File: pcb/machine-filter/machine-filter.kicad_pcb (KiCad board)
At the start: 2 copper layers, 150 x 107 mm, 156 parts, among them J1 PJ398SM, J10 PJ398SM, J11 PJ398SM, J12 PJ398SM, J13 EURO PWR 2x5, J14 EXPANSION 2x4, J15 TF-01A, J2 PJ398SM, J3 PJ398SM, J4 PJ398SM, J5 PJ398SM, J6 PJ398SM, J7 PJ398SM, J8 PJ398SM, J9 PJ398SM, U1 LMV324, U2 LMV324, U3 TL072, U4 TL072, U5 LM4040-10, U6 74HC4051, U7 LM324, U8 LM324

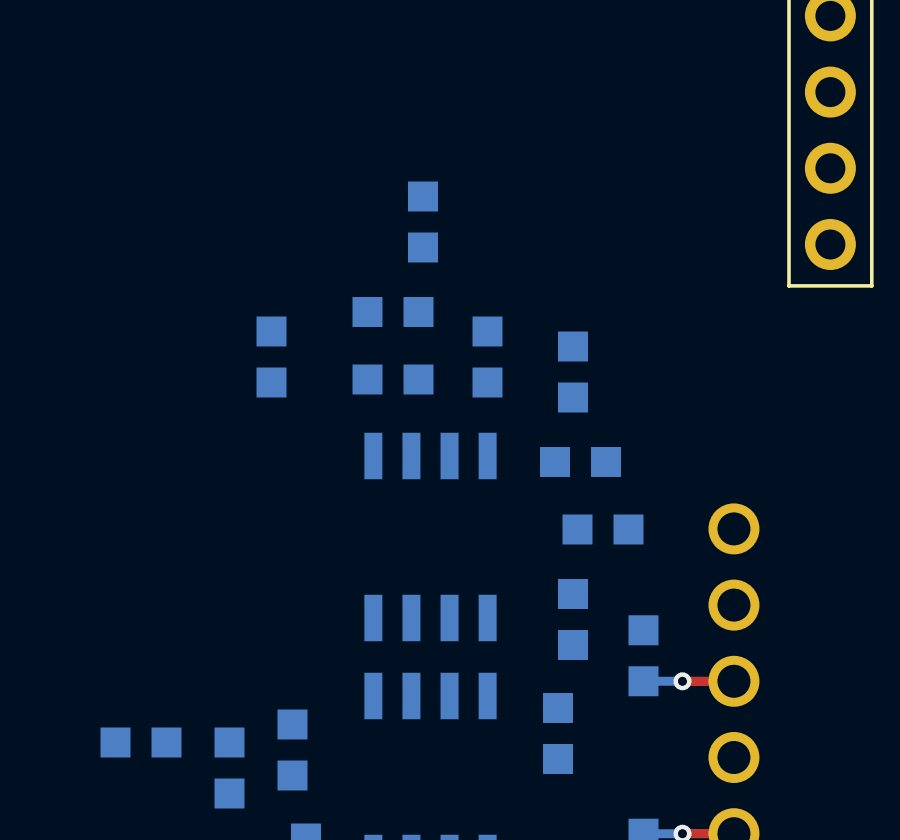
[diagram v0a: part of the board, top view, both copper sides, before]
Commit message: Section audio out (U4) by pattern; render_board.py for whole-board pictures
Co-Authored-By: Claude Opus 5.5 <noreply@anthropic.com>
Claude-Session: https://claude.ai/code/session_01Cf5qNBi3oNHhbCjPHvswth
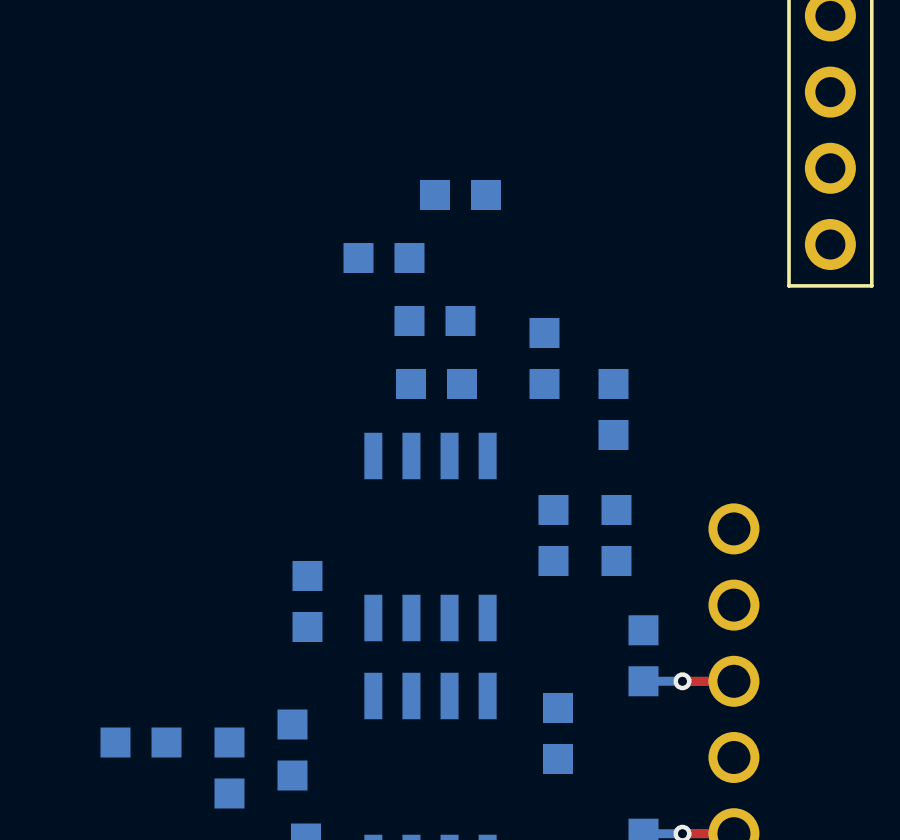
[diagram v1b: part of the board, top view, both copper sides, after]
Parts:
- moved R64 9.44 mm to (201.9, 82.2), turned to 0 degrees
- moved C73 8.24 mm to (199.4, 93.7)
- moved R61 2.87 mm to (207.6, 91.5), turned to -90 degrees
- moved C72 1.90 mm to (207.3, 85.5), turned to -90 degrees
- moved R62 1.84 mm to (209.6, 87.2)
- moved R66 1.54 mm to (204.5, 80.1), turned to 0 degrees
- moved R65 1.46 mm to (203.7, 86.4)
- moved C62 1.43 mm to (203.7, 84.3)
- moved C60 0.49 mm to (209.7, 91.5), turned to -90 degrees

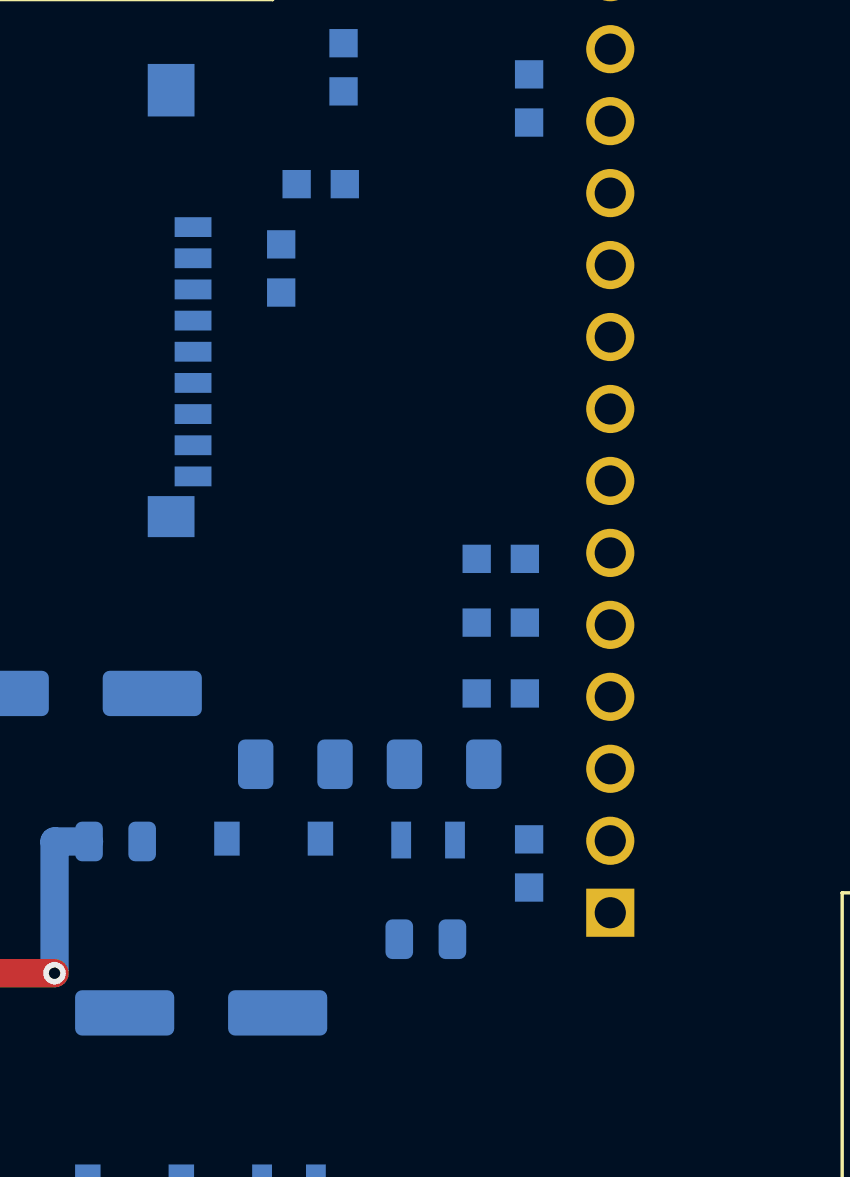
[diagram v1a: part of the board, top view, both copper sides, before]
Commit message: Section microSD: pull-ups as a column beside the Seed3 SD pins, C100 at J15's supply pin
Co-Authored-By: Claude Opus 5.5 <noreply@anthropic.com>
Claude-Session: https://claude.ai/code/session_01Cf5qNBi3oNHhbCjPHvswth
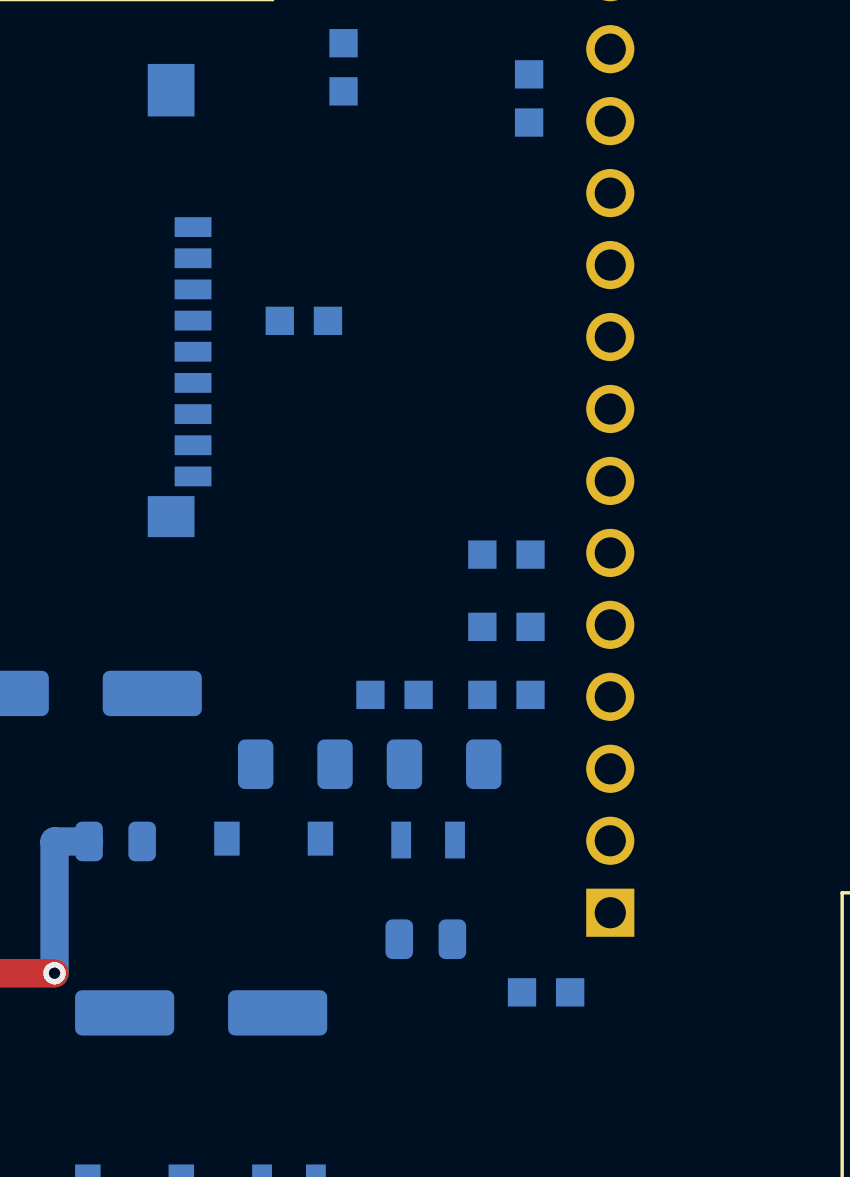
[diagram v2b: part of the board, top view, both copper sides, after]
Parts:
- moved R100 15.6 mm to (206.0, 131.8), turned to 180 degrees
- moved C100 4.86 mm to (202.8, 118.6)
- moved R101 4.59 mm to (211.3, 142.3), turned to 180 degrees
- moved R102 0.25 mm to (209.9, 126.8)
- moved R103 0.25 mm to (209.9, 129.4)
- moved R104 0.21 mm to (209.9, 131.8)
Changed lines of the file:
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@@
 	(footprint "filter-module:R_0603"
 		(layer "B.Cu")
-		(at 209.75 131.75 180)
+		(at 209.95 131.8 180)
 		(descr "Resistor SMD 0603, reflow soldering, Vishay (see dcrcw.pdf)")
 		(tags "resistor 0603")
@@
 	(footprint "filter-module:C_0603"
 		(layer "B.Cu")
-		(at 203.395 113.775)
+		(at 202.8 118.6)
 		(descr "Capacitor SMD 0603, reflow soldering, AVX (see smccp.pdf)")
 		(tags "capacitor 0603 C0603")
@@
 	(footprint "filter-module:R_0603"
 		(layer "B.Cu")
-		(at 209.75 127 180)
+		(at 209.95 126.85 180)
 		(descr "Resistor SMD 0603, reflow soldering, Vishay (see dcrcw.pdf)")
 		(tags "resistor 0603")
@@
 	(footprint "filter-module:R_0603"
 		(layer "B.Cu")
-		(at 209.75 129.25 180)
+		(at 209.95 129.4 180)
 		(descr "Resistor SMD 0603, reflow soldering, Vishay (see dcrcw.pdf)")
 		(tags "resistor 0603")
@@
 	(footprint "filter-module:R_0603"
 		(layer "B.Cu")
-		(at 202 116.75 -90)
+		(at 206 131.8 180)
 		(descr "Resistor SMD 0603, reflow soldering, Vishay (see dcrcw.pdf)")
 		(tags "resistor 0603")
 		(property "Reference" "R100"
-			(at 0 1.449999 90)
+			(at 0 1.449999 0)
 			(unlocked yes)
 			(layer "B.SilkS")
@@
 		)
 		(property "Value" "47k"
-			(at 0 -1.45 90)
+			(at 0 -1.45 0)
 			(unlocked yes)
 			(layer "B.SilkS")
@@
 		)
 		(property "Datasheet" ""
-			(at 0 0 90)
+			(at 0 0 0)
 			(layer "B.Fab")
 			(hide yes)
@@
 		)
 		(property "Description" ""
-			(at 0 0 90)
+			(at 0 0 0)
 			(layer "B.Fab")
 			(hide yes)
@@
 		(duplicate_pad_numbers_are_jumpers no)
 		(fp_line
-			(start -0.85 0.699999)
-			(end 0.85 0.699999)
+			(start 0.85 -0.7)
+			(end -0.85 -0.7)
 			(stroke
 				(width 0.12)
@@
 		)
 		(fp_line
-			(start 0.85 -0.7)
-			(end -0.85 -0.7)
+			(start -0.85 0.699999)
+			(end 0.85 0.699999)
 			(stroke
 				(width 0.12)
@@
 		)
 		(fp_line
-			(start -1.6 0.75)
-			(end 1.6 0.75)
+			(start 1.6 0.75)
+			(end 1.6 -0.75)
 			(stroke
 				(width 0.05)
@@
 		(fp_line
 			(start -1.6 0.75)
-			(end -1.6 -0.75)
+			(end 1.6 0.75)
 			(stroke
 				(width 0.05)
@@
 		)
 		(fp_line
-			(start 1.6 0.75)
-			(end 1.6 -0.75)
+			(start -1.6 0.75)
+			(end -1.6 -0.75)
 			(stroke
 				(width 0.05)
@@
 		)
 		(pad "1" smd rect
-			(at -0.85 0 270)
+			(at -0.85 0 180)
 			(size 1 1)
 			(layers "B.Cu" "B.Mask" "B.Paste")
@@
 		)
 		(pad "2" smd rect
-			(at 0.85 0 270)
+			(at 0.85 0 180)
 			(size 1 1)
 			(layers "B.Cu" "B.Mask" "B.Paste")
@@
 	(footprint "filter-module:R_0603"
 		(layer "B.Cu")
-		(at 210.75 137.75 -90)
+		(at 211.35 142.3 180)
 		(descr "Resistor SMD 0603, reflow soldering, Vishay (see dcrcw.pdf)")
 		(tags "resistor 0603")
 		(property "Reference" "R101"
-			(at 0 1.449999 90)
+			(at 0 1.449999 0)
 			(unlocked yes)
 			(layer "B.SilkS")
@@
 		)
 		(property "Value" "47k"
-			(at 0 -1.45 90)
+			(at 0 -1.45 0)
 			(unlocked yes)
 			(layer "B.SilkS")
@@
 		)
 		(property "Datasheet" ""
-			(at 0 0 90)
+			(at 0 0 0)
 			(layer "B.Fab")
 			(hide yes)
@@
 		)
 		(property "Description" ""
-			(at 0 0 90)
+			(at 0 0 0)
 			(layer "B.Fab")
 			(hide yes)
@@
 		(duplicate_pad_numbers_are_jumpers no)
 		(fp_line
-			(start -0.85 0.699999)
-			(end 0.85 0.699999)
+			(start 0.85 -0.7)
+			(end -0.85 -0.7)
 			(stroke
 				(width 0.12)
@@
 		)
 		(fp_line
-			(start 0.85 -0.7)
-			(end -0.85 -0.7)
+			(start -0.85 0.699999)
+			(end 0.85 0.699999)
 			(stroke
 				(width 0.12)
@@
 		)
 		(fp_line
-			(start -1.6 0.75)
-			(end 1.6 0.75)
+			(start 1.6 0.75)
+			(end 1.6 -0.75)
 			(stroke
 				(width 0.05)
@@
 		(fp_line
 			(start -1.6 0.75)
-			(end -1.6 -0.75)
+			(end 1.6 0.75)
 			(stroke
 				(width 0.05)
@@
 		)
 		(fp_line
-			(start 1.6 0.75)
-			(end 1.6 -0.75)
+			(start -1.6 0.75)
+			(end -1.6 -0.75)
 			(stroke
 				(width 0.05)
@@
 		)
 		(pad "1" smd rect
-			(at -0.85 0 270)
+			(at -0.85 0 180)
 			(size 1 1)
 			(layers "B.Cu" "B.Mask" "B.Paste")
@@
 		)
 		(pad "2" smd rect
-			(at 0.85 0 270)
+			(at 0.85 0 180)
 			(size 1 1)
 			(layers "B.Cu" "B.Mask" "B.Paste")

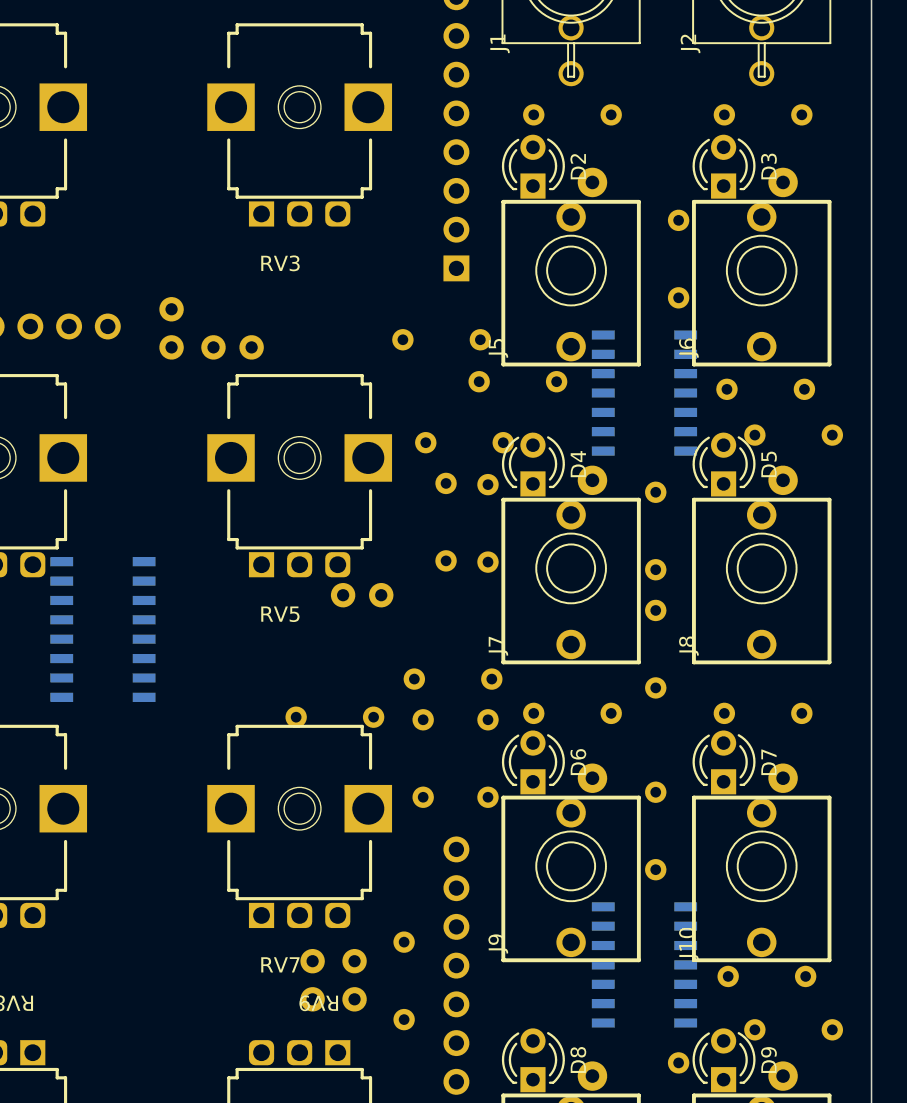
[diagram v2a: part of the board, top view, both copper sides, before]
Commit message: Control sections U6 and U7: decouplers at their supply pins; U7's resistors re-placed around them
The bank pattern doesn't fit between the jacks (parts landed 6-14 mm off), so U7's resistors keep the
shortest-connection placement (auto_place), re-run after the decouplers moved.

Co-Authored-By: Claude Opus 5.5 <noreply@anthropic.com>
Claude-Session: https://claude.ai/code/session_01Cf5qNBi3oNHhbCjPHvswth
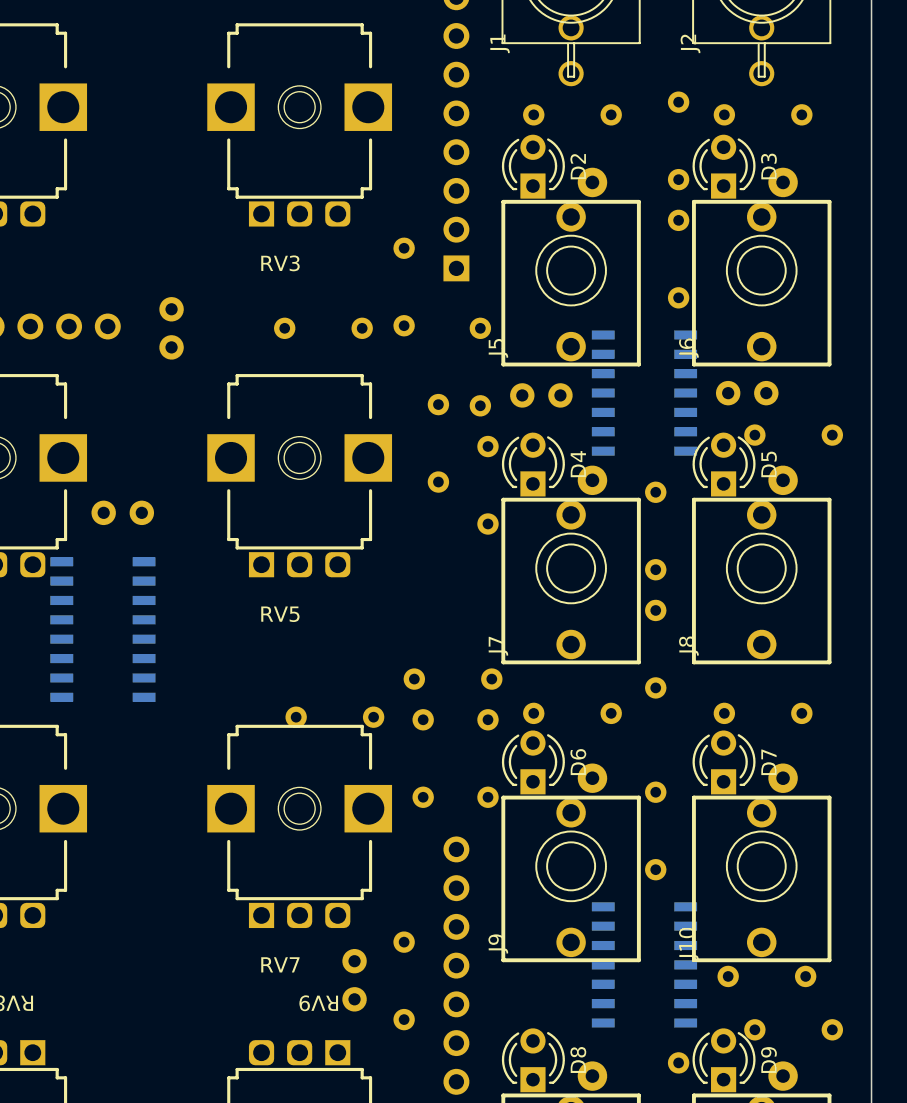
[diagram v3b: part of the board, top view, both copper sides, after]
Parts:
- moved C82 39.6 mm to (147.5, 110.4), turned to 0 degrees
- moved C81 33.9 mm to (161.0, 110.2)
- moved R83 20.7 mm to (139.8, 100.8), turned to -90 degrees
- moved C80 16.6 mm to (120.0, 118.1)
- moved R93 13.2 mm to (137.0, 106.0), turned to 180 degrees
- moved R81 10.2 mm to (157.8, 104.0), turned to 90 degrees
- moved R91 7.75 mm to (157.8, 96.2)
- moved R80 6.10 mm to (144.8, 106.0), turned to -90 degrees
- moved R90 5.06 mm to (142.0, 111.0), turned to -90 degrees
- moved R73 1.03 mm to (145.2, 113.8), turned to -90 degrees

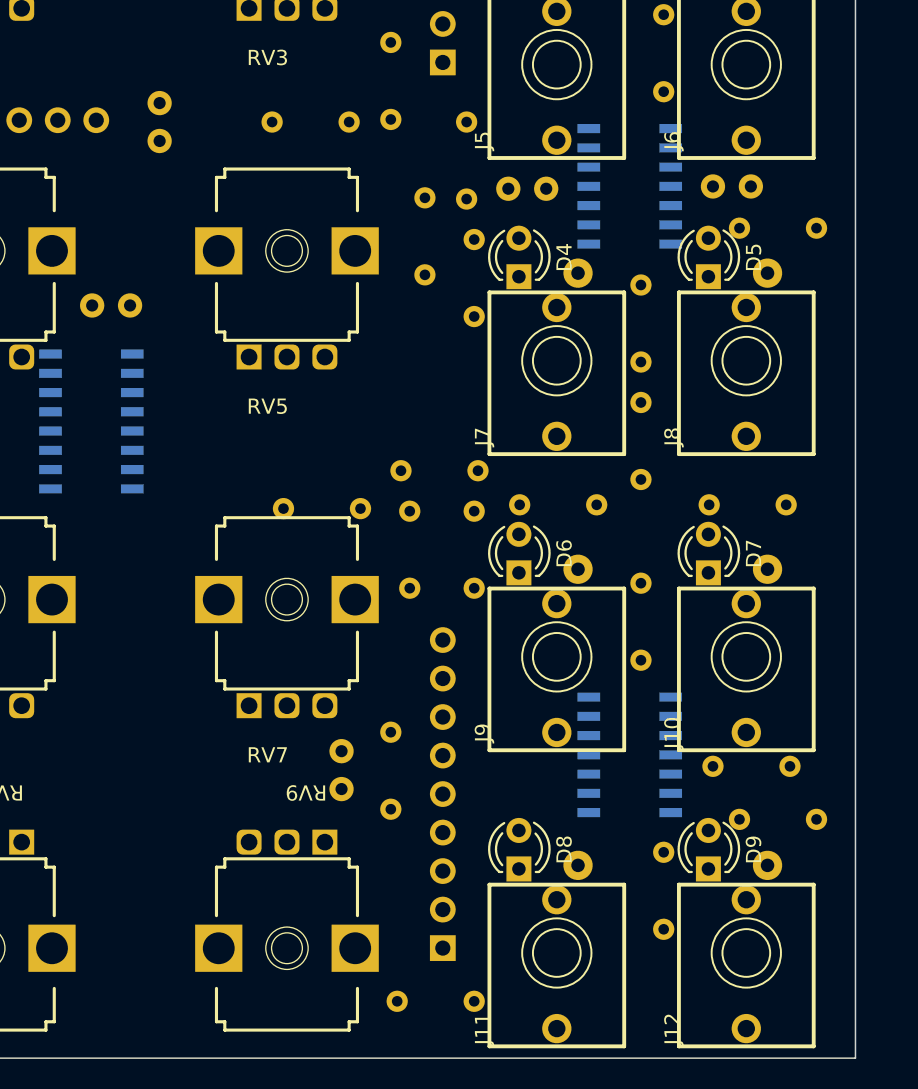
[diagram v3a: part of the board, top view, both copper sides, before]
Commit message: Control section U8: decouplers at its supply pins; its resistors re-placed around them
Co-Authored-By: Claude Opus 5.5 <noreply@anthropic.com>
Claude-Session: https://claude.ai/code/session_01Cf5qNBi3oNHhbCjPHvswth
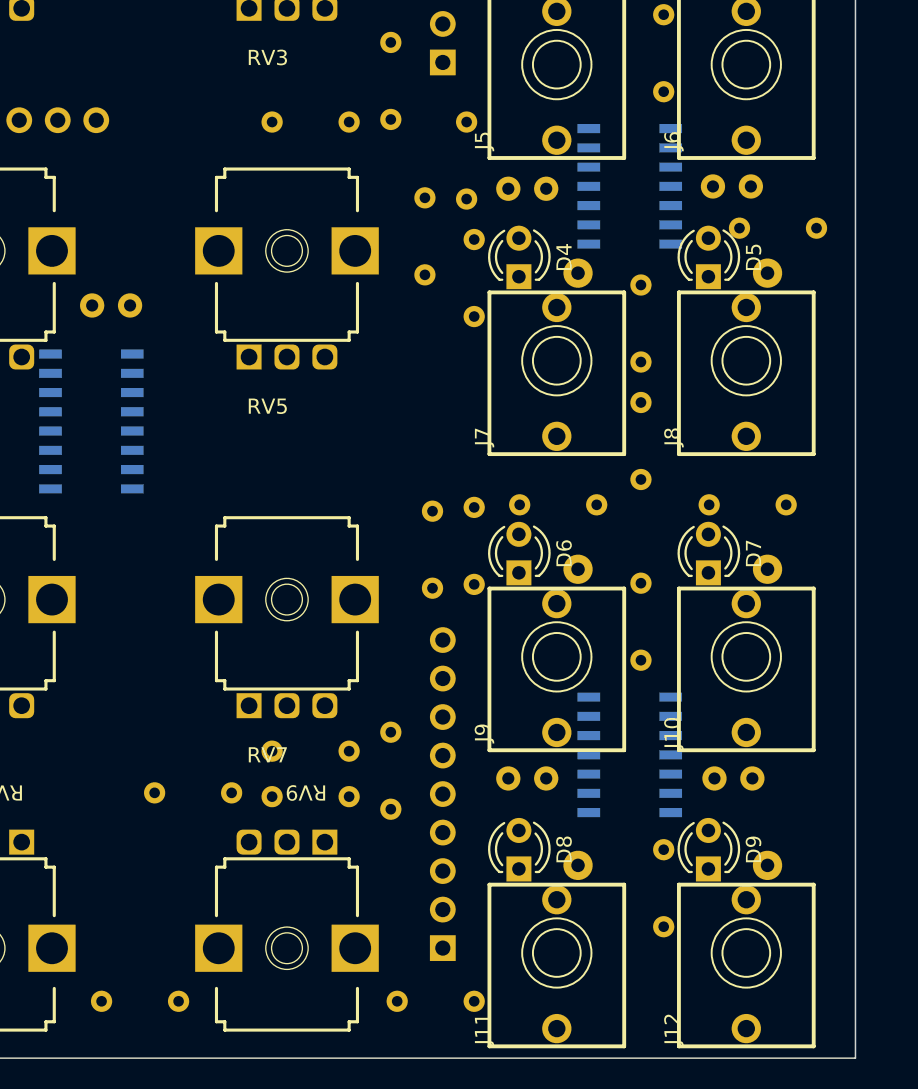
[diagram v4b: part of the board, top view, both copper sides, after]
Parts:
- moved C83 55.7 mm to (161.1, 149.3), turned to 0 degrees
- moved R97 40.2 mm to (125.8, 164.0)
- moved R78 26.1 mm to (137.0, 147.5), turned to 180 degrees
- moved R96 17.9 mm to (129.2, 150.2), turned to 180 degrees
- moved R77 15.8 mm to (137.0, 150.5)
- moved R87 13.4 mm to (145.2, 164.0), turned to 180 degrees
- moved C84 11.1 mm to (147.5, 149.3), turned to 0 degrees
- moved R95 7.08 mm to (142.5, 136.8), turned to 90 degrees
- moved R85 6.39 mm to (157.8, 154.0), turned to -90 degrees
- moved R94 0.25 mm to (145.2, 136.5)
